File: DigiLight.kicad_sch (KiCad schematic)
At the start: 83 parts, among them IC1 MAX9814 Module, J1 IN_1, J2 IN_2, J3 POWER (5V/3A), J4 APU-2, J5 112J-TDAR-R-Micro_SD_Card, J6 WS2811, Q1 BC846, Q2 BC846, Q3 IRLML6402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

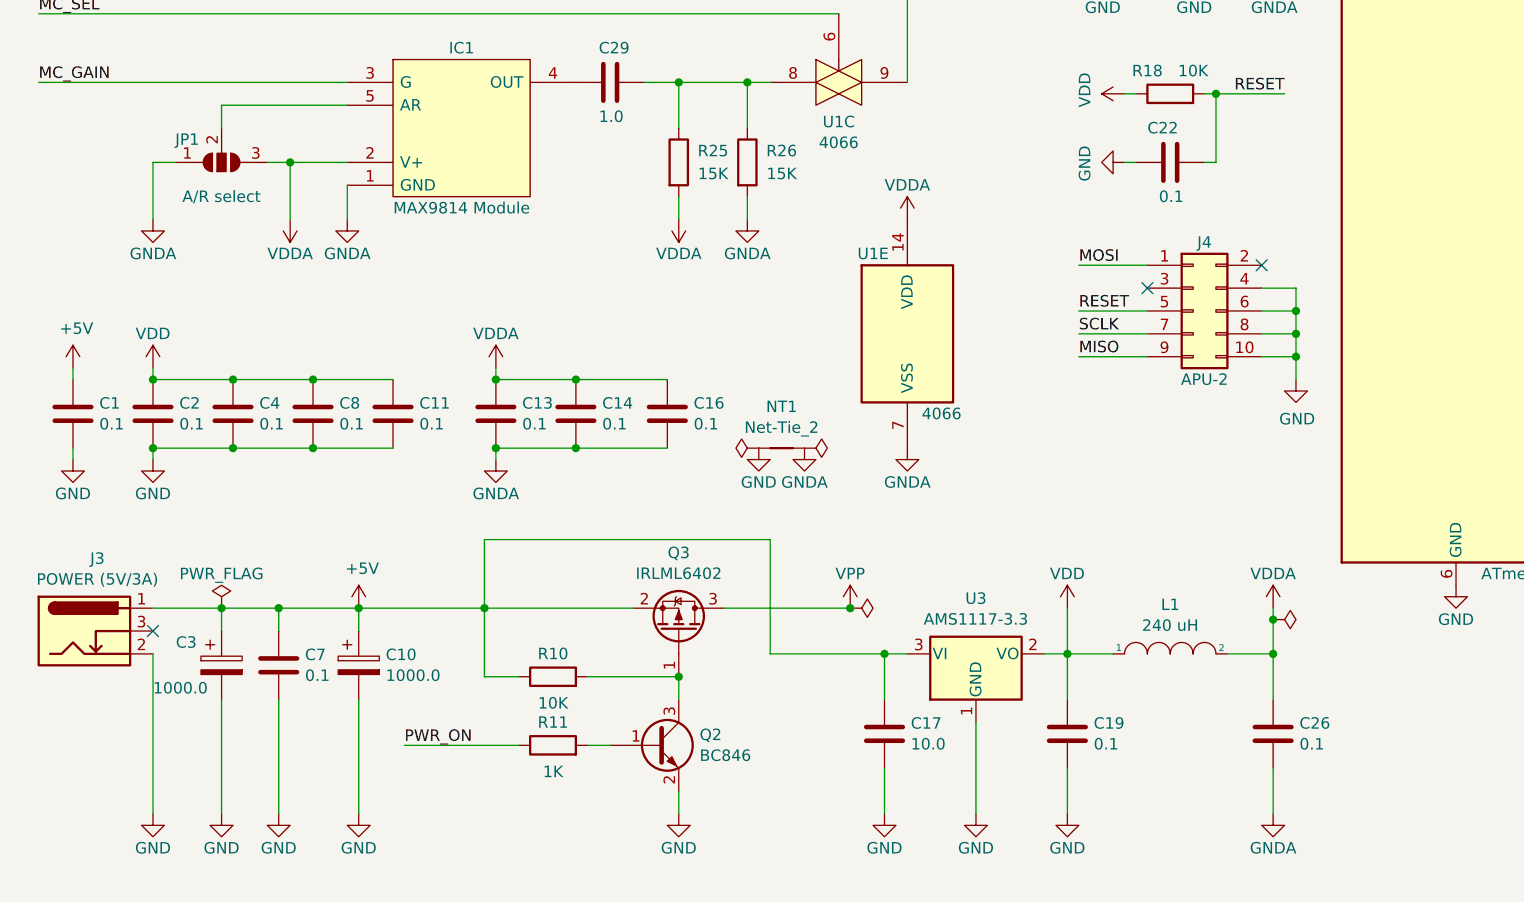
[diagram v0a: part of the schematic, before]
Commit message: Power connector replaced to USB type-c
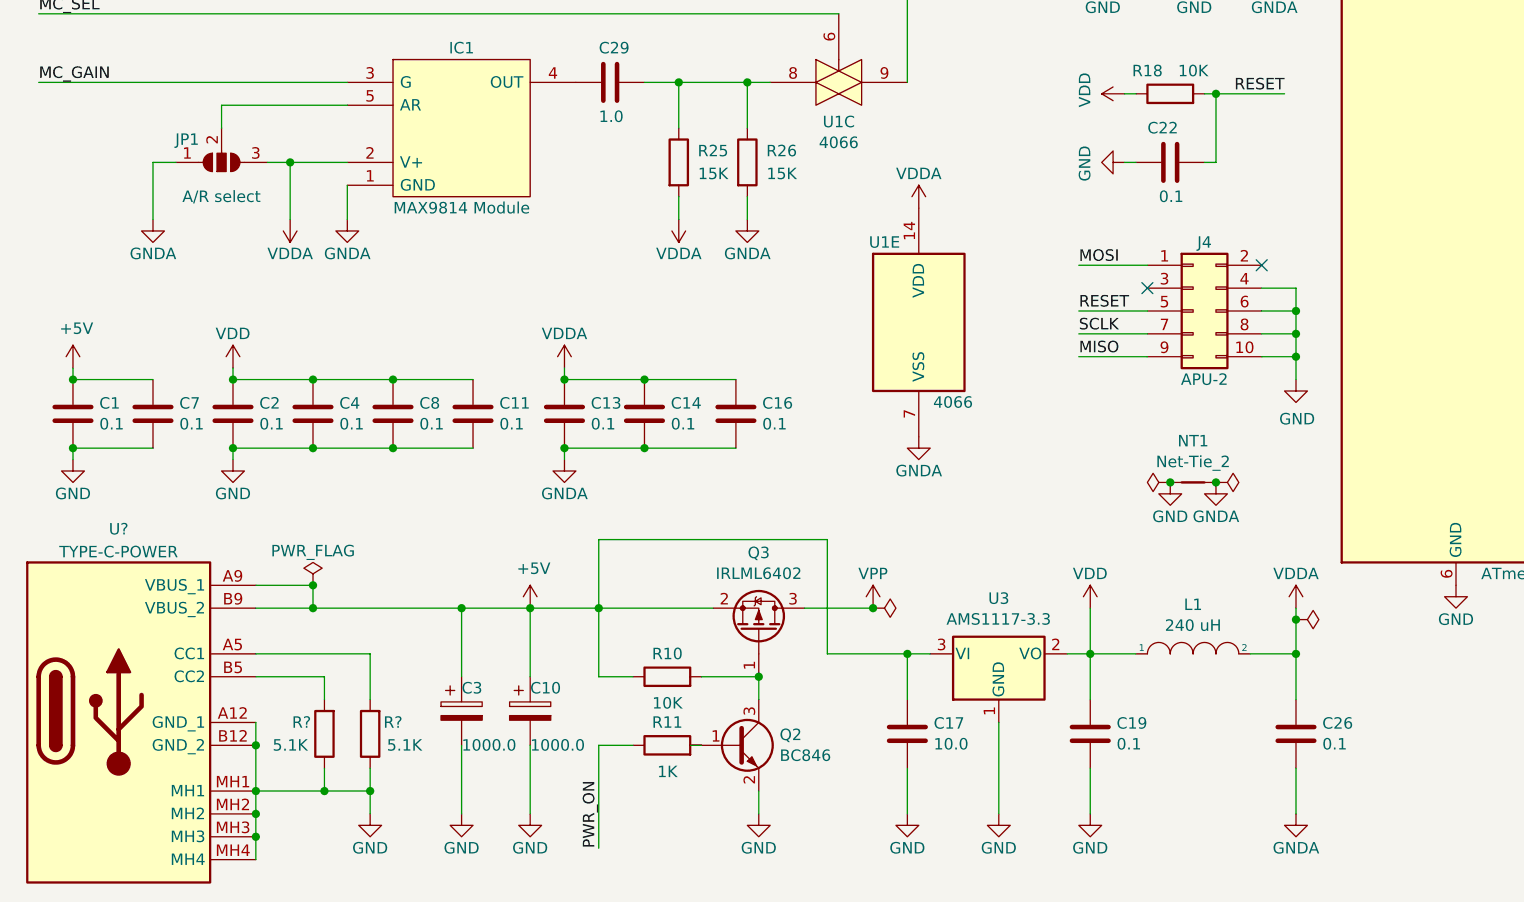
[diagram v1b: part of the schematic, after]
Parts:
- removed J3: POWER (5V/3A), ExternalLib:DC-044, symbol Connector:Barrel_Jack_Switch
- added R? (x2): 5.1K, Resistor_SMD:R_1206_3216Metric, symbol Device:R
- added U?: TYPE-C-POWER, ExternalLib:TYPEC31M17, symbol TypeC-31-M-17:TYPE-C-POWER
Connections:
- net +5V: now also U?.A9 (VBUS_1), U?.B9 (VBUS_2)
- net GND: now also R?.1, R?.1, U?.A12 (GND_1), U?.B12 (GND_2), U?.MH1, U?.MH2, U?.MH3, U?.MH4
- new net: R?.2, U?.A5 (CC1)
- new net: R?.2, U?.B5 (CC2)
- no-connect marks 14 -> 13
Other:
- moved on the sheet: C10, C11, C13, C14, C16, C17, C19, C2, C26, C3, C4, C7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
